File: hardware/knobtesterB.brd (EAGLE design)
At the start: 30.5 x 41.4 mm, 6 parts

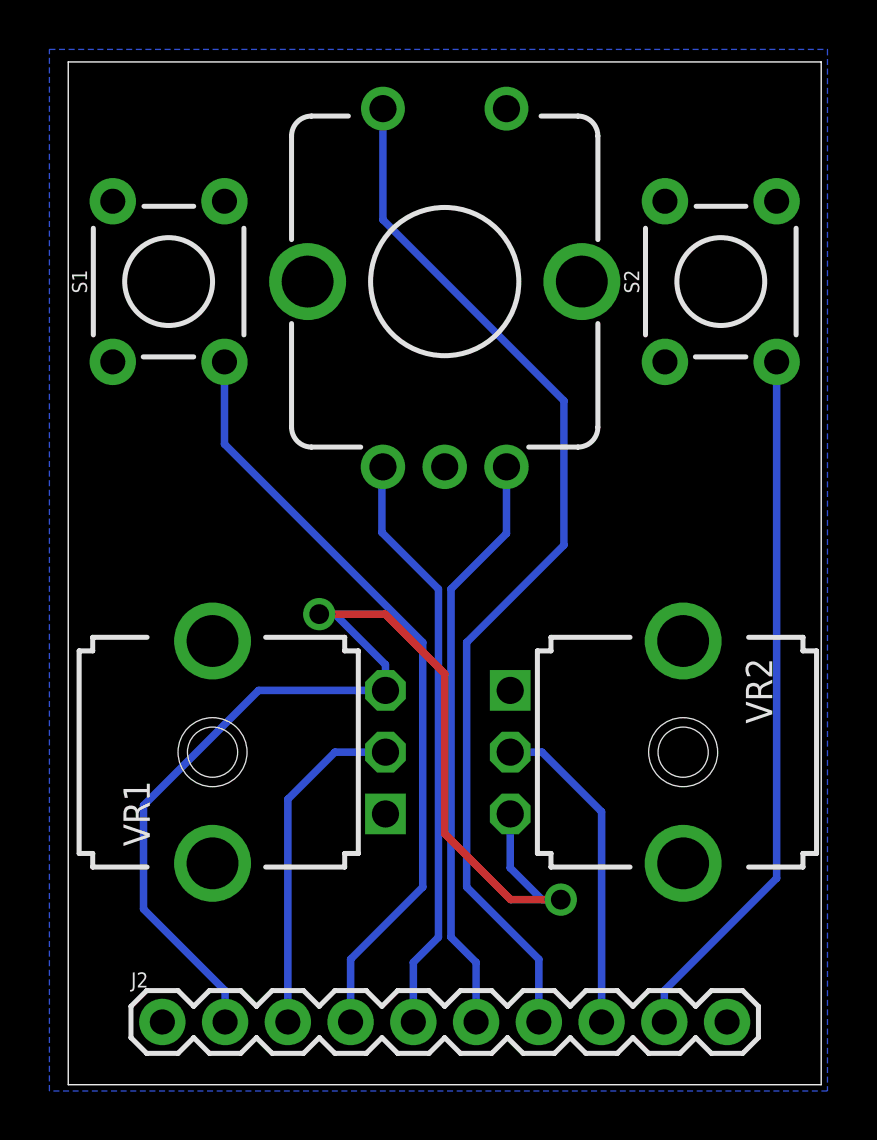
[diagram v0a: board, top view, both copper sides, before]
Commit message: cleaned up UI after knobtesterA results
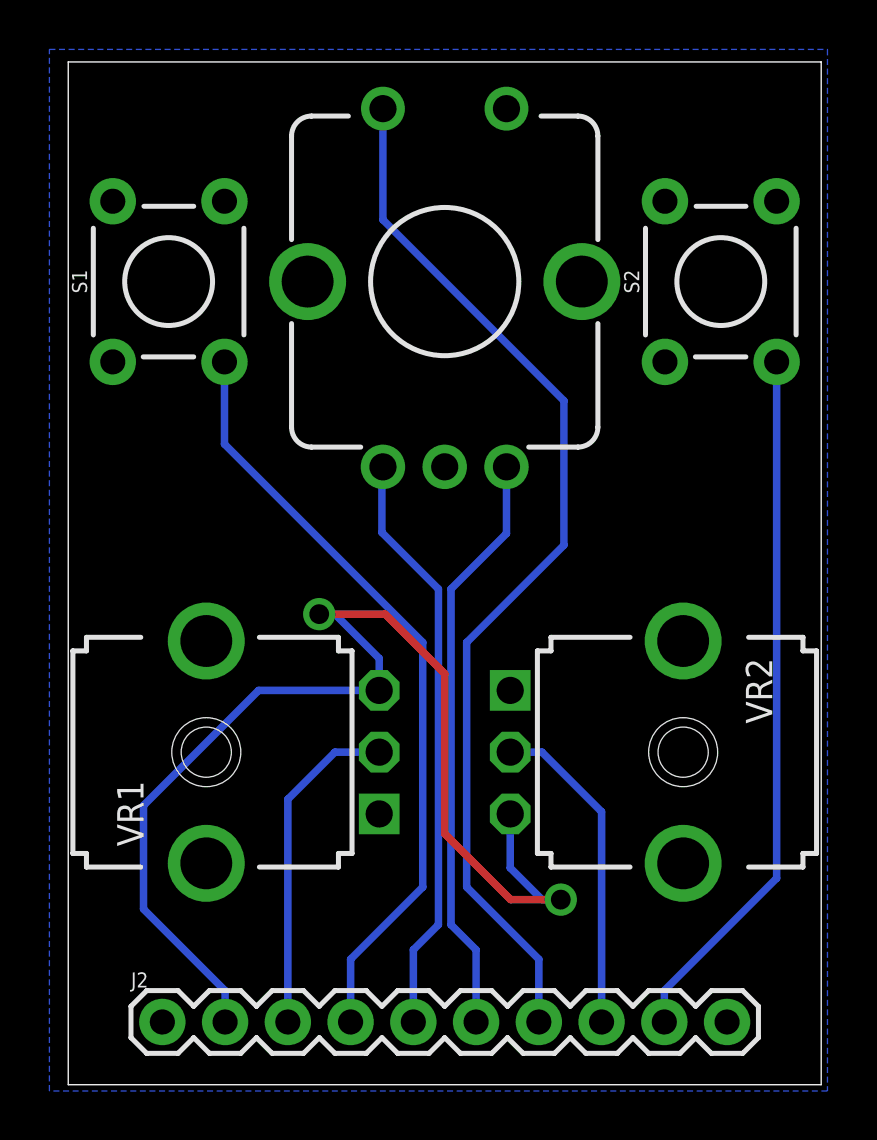
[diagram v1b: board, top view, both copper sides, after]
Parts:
- moved VR1 0.25 mm to (5.59, 13.5)
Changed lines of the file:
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@@
 <dimension x1="31.496" y1="41.656" x2="33.528" y2="32.512" x3="37.211" y3="37.084" textsize="1.016" layer="47" dtype="vertical" width="0.0254" unit="inch" visible="yes"/>
 <dimension x1="37.846" y1="32.512" x2="32.766" y2="13.462" x3="43.561" y3="22.987" textsize="1.016" layer="47" dtype="vertical" width="0.0254" unit="inch" visible="yes"/>
-<dimension x1="24.892" y1="14.986" x2="5.842" y2="15.24" x3="15.367" y3="21.971" textsize="1.016" layer="47" dtype="horizontal" width="0.0254" unit="inch" visible="yes"/>
-<dimension x1="25.654" y1="20.574" x2="6.604" y2="20.828" x3="16.129" y3="27.559" textsize="1.016" layer="47" dtype="horizontal" width="0.0254" unit="inch" visible="yes"/>
+<dimension x1="24.892" y1="14.986" x2="5.588" y2="15.24" x3="15.24" y3="27.305" textsize="1.016" layer="47" dtype="horizontal" width="0.0254" unit="inch" visible="yes"/>
 <dimension x1="25.908" y1="34.036" x2="4.318" y2="35.56" x3="15.113" y3="42.545" textsize="1.016" layer="47" dtype="horizontal" width="0.0254" unit="inch" visible="yes"/>
 </plain>
@@
 </element>
 <element name="U$1" library="halcyonmod_Switches" package="ENCODER_SW" override_package3d_urn="urn:adsk.eagle:package:22891623/2" override_package_urn="urn:adsk.eagle:footprint:22891624/1" value="ENCODER_SW" x="15.24" y="32.512" smashed="yes"/>
-<element name="VR1" library="MusicThingModular" package="9MM_SNAP-IN_POT" override_package3d_urn="urn:adsk.eagle:package:22891957/2" override_package_urn="urn:adsk.eagle:footprint:22891958/1" value="" x="5.842" y="13.462" smashed="yes" rot="R90">
-<attribute name="NAME" x="3.302" y="9.652" size="1.0668" layer="25" rot="R90"/>
-<attribute name="VALUE" x="9.652" y="9.652" size="1.27" layer="27" rot="R90"/>
+<element name="VR1" library="MusicThingModular" package="9MM_SNAP-IN_POT" override_package3d_urn="urn:adsk.eagle:package:22891957/2" override_package_urn="urn:adsk.eagle:footprint:22891958/1" value="" x="5.588" y="13.462" smashed="yes" rot="R90">
+<attribute name="NAME" x="3.048" y="9.652" size="1.0668" layer="25" rot="R90"/>
+<attribute name="VALUE" x="9.398" y="9.652" size="1.27" layer="27" rot="R90"/>
 </element>
 <element name="VR2" library="MusicThingModular" package="9MM_SNAP-IN_POT" override_package3d_urn="urn:adsk.eagle:package:22891949/2" override_package_urn="urn:adsk.eagle:footprint:22891950/1" value="" x="24.892" y="13.462" smashed="yes" rot="R270">
@@
 <contactref element="VR2" pad="3"/>
 <via x="10.16" y="19.05" extent="1-16" drill="0.8"/>
-<wire x1="12.842" y1="17.003" x2="10.795" y2="19.05" width="0.3048" layer="16"/>
+<wire x1="12.588" y1="17.257" x2="10.795" y2="19.05" width="0.3048" layer="16"/>
 <wire x1="10.16" y1="19.05" x2="10.795" y2="19.05" width="0.3048" layer="16"/>
-<wire x1="12.842" y1="17.003" x2="12.842" y2="15.962" width="0.3048" layer="16"/>
+<wire x1="12.588" y1="17.257" x2="12.588" y2="15.962" width="0.3048" layer="16"/>
 <contactref element="J2" pad="2"/>
-<wire x1="7.707" y1="15.962" x2="12.842" y2="15.962" width="0.3048" layer="16"/>
+<wire x1="7.707" y1="15.962" x2="12.588" y2="15.962" width="0.3048" layer="16"/>
 <wire x1="17.892" y1="10.962" x2="17.892" y2="8.778" width="0.3048" layer="16"/>
 <wire x1="19.177" y1="7.493" x2="17.892" y2="8.778" width="0.3048" layer="16"/>
@@
 <contactref element="VR1" pad="2"/>
 <contactref element="J2" pad="3"/>
-<wire x1="10.795" y1="13.462" x2="12.842" y2="13.462" width="0.3048" layer="16"/>
+<wire x1="10.795" y1="13.462" x2="12.588" y2="13.462" width="0.3048" layer="16"/>
 <wire x1="8.89" y1="11.557" x2="10.795" y2="13.462" width="0.3048" layer="16"/>
 <wire x1="8.89" y1="11.557" x2="8.89" y2="2.54" width="0.3048" layer="16"/>
@@
 <contactref element="U$1" pad="A"/>
 <contactref element="J2" pad="5"/>
-<wire x1="14.986" y1="20.066" x2="14.986" y2="5.969" width="0.3048" layer="16"/>
-<wire x1="13.97" y1="2.54" x2="13.97" y2="4.953" width="0.3048" layer="16"/>
-<wire x1="14.986" y1="5.969" x2="13.97" y2="4.953" width="0.3048" layer="16"/>
+<wire x1="14.986" y1="20.066" x2="14.986" y2="6.477" width="0.3048" layer="16"/>
+<wire x1="13.97" y1="2.54" x2="13.97" y2="5.461" width="0.3048" layer="16"/>
+<wire x1="14.986" y1="6.477" x2="13.97" y2="5.461" width="0.3048" layer="16"/>
 <wire x1="14.986" y1="20.066" x2="12.7" y2="22.352" width="0.3048" layer="16"/>
 <wire x1="12.7" y1="22.352" x2="12.7" y2="24.972" width="0.3048" layer="16"/>
@@
 <wire x1="17.74" y1="22.312" x2="15.494" y2="20.066" width="0.3048" layer="16"/>
 <contactref element="J2" pad="6"/>
-<wire x1="15.494" y1="20.066" x2="15.494" y2="5.969" width="0.3048" layer="16"/>
-<wire x1="16.51" y1="4.953" x2="15.494" y2="5.969" width="0.3048" layer="16"/>
-<wire x1="16.51" y1="4.953" x2="16.51" y2="2.54" width="0.3048" layer="16"/>
+<wire x1="15.494" y1="20.066" x2="15.494" y2="6.477" width="0.3048" layer="16"/>
+<wire x1="16.51" y1="5.461" x2="15.494" y2="6.477" width="0.3048" layer="16"/>
+<wire x1="16.51" y1="5.461" x2="16.51" y2="2.54" width="0.3048" layer="16"/>
 <wire x1="17.74" y1="22.312" x2="17.74" y2="25.012" width="0.3048" layer="16"/>
 </signal>
